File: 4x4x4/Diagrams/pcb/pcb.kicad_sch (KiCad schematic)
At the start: 78 parts, among them J1 Conn_01x04_Female, J10 Conn_01x04_Female, J11 Conn_01x04_Female, J12 Conn_01x04_Female, J13 Conn_01x04_Female, J14 Conn_01x04_Female, J2 Conn_01x06_Female, J3 Conn_01x04_Female, J4 Conn_01x04_Female, J5 Conn_01x04_Female, J6 Conn_01x04_Female, J7 Conn_01x04_Female, J8 Conn_01x04_Female, J9 Conn_01x04_Female, Q1 2N2219, Q2 2N2219, Q3 2N2219, Q4 2N2219, U1 74HC595, U2 74HC595, U3 74HC595, U4 74HC595, U5 74HC595, U6 74HC595, U7 74HC595

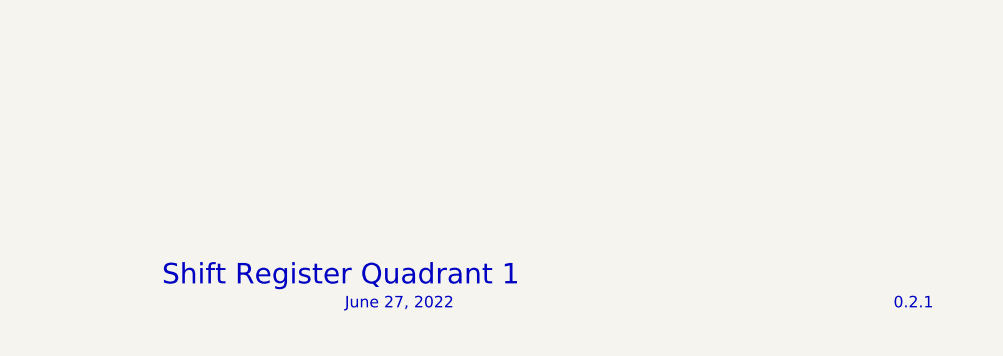
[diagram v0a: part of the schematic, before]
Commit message: revised quad 1 diagram
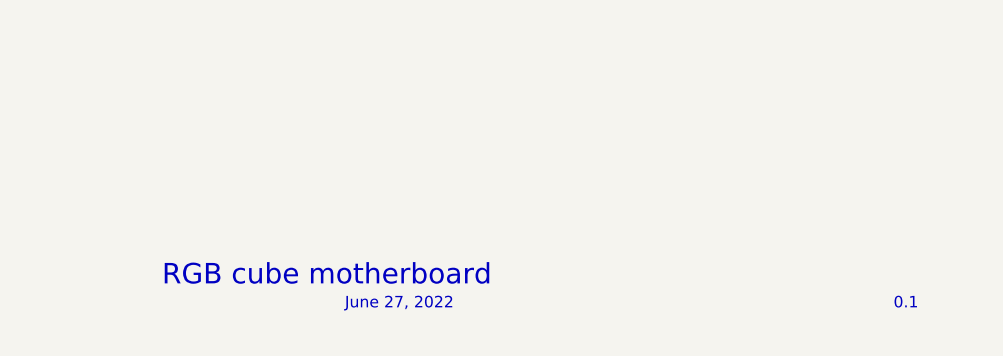
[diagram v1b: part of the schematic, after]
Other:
- note added: "0.1"
- note added: "RGB cube motherboard"
- note removed: "0.2.1"
- note removed: "Shift Register Quadrant 1"
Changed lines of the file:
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@@
     (stroke (width 0) (type default) (color 0 0 0 0))
   )
-  (text "Shift Register Quadrant 1 " (at 187.96 191.77 0)
+  (text "RGB cube motherboard" (at 187.96 191.77 0)
     (effects (font (size 2.27 2.27)) (justify left bottom))
   )
@@
     (effects (font (size 1.27 1.27)) (justify left bottom))
   )
-  (text "0.2.1" (at 269.24 194.31 0)
+  (text "0.1" (at 269.24 194.31 0)
     (effects (font (size 1.27 1.27)) (justify left bottom))
   )

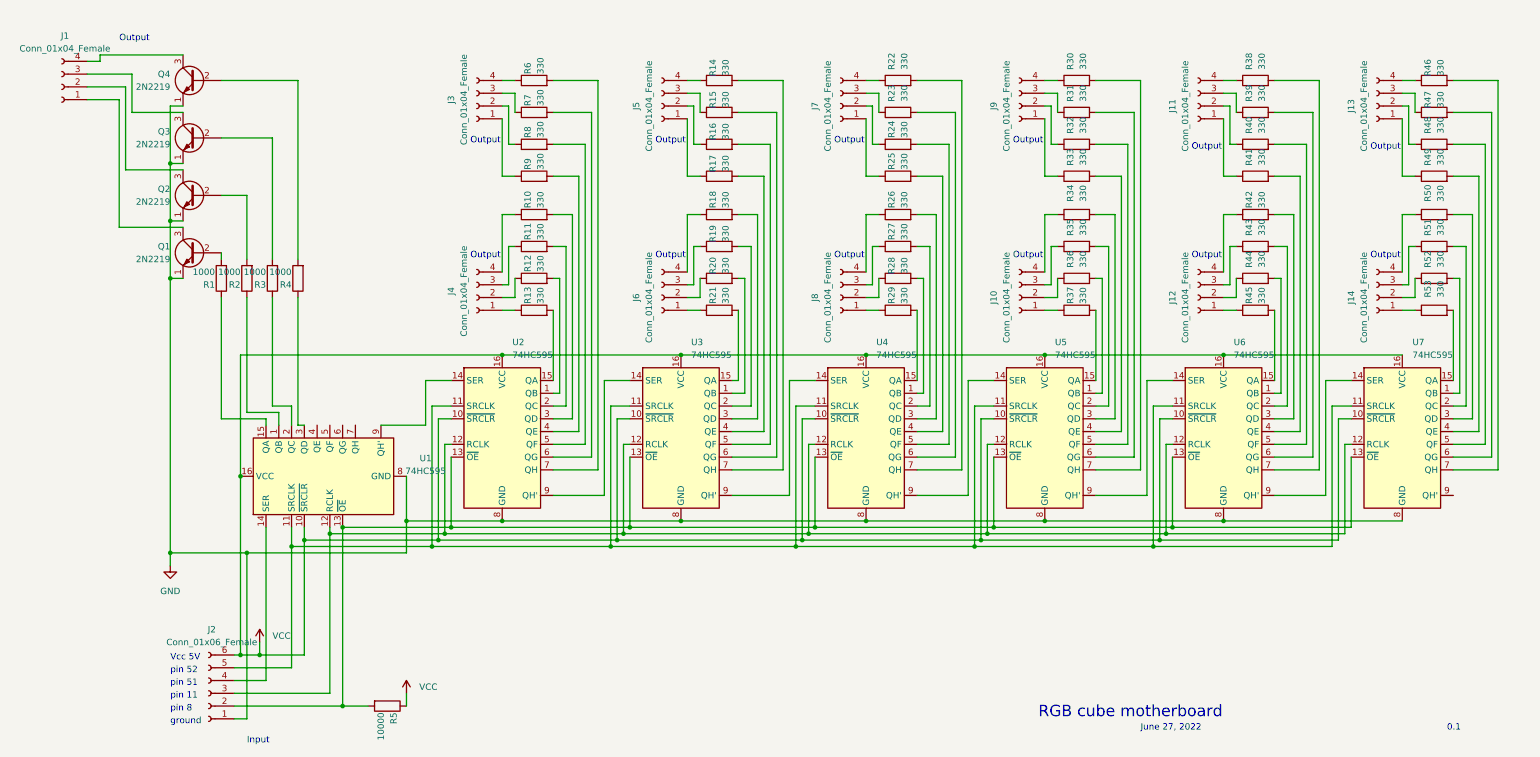
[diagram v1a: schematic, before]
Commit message: laying out 3d model of pcb
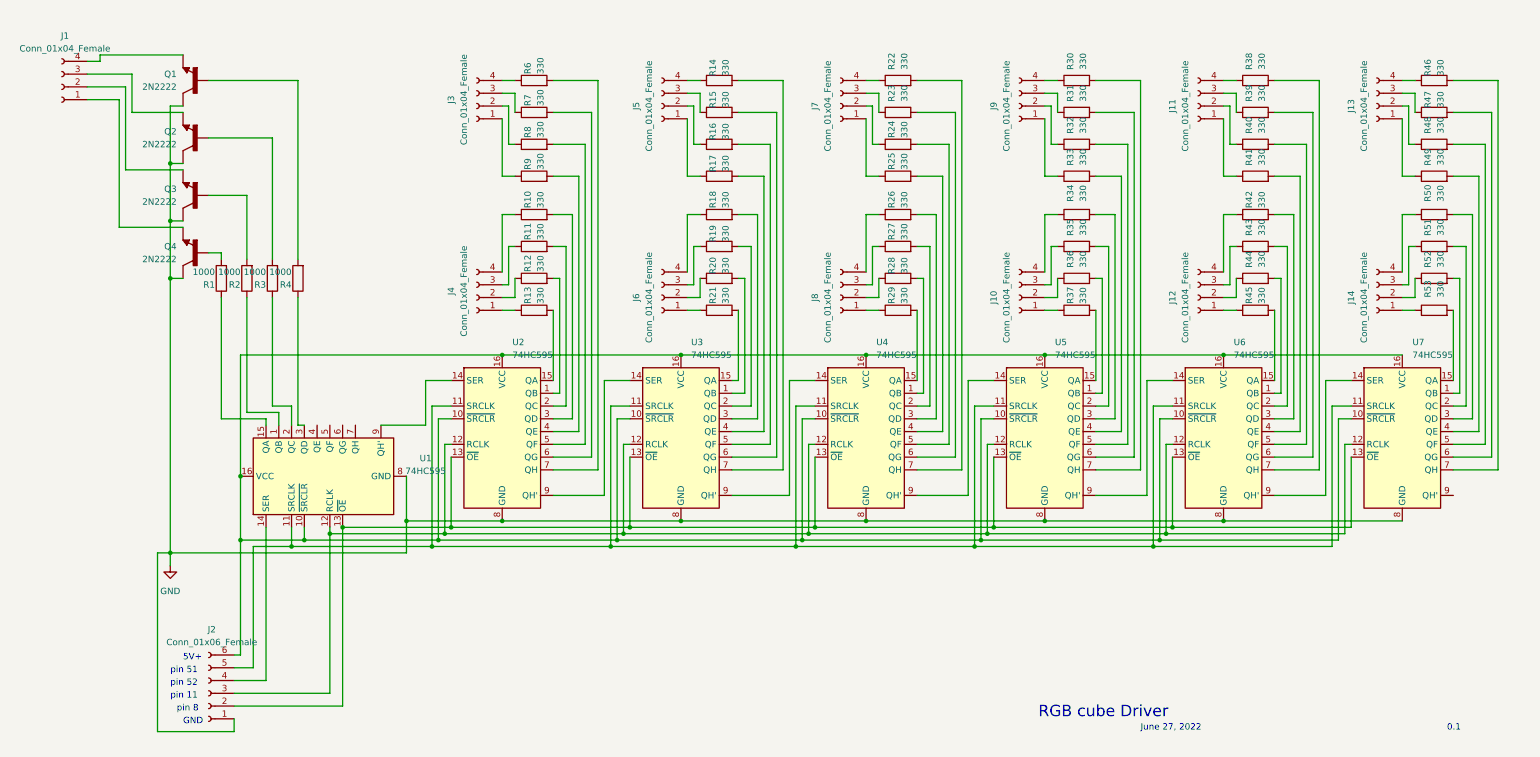
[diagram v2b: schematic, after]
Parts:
- removed Q1, Q2, Q3, Q4: 2N2219, Package_TO_SOT_THT:TO-39-3, symbol Transistor_BJT:2N2219
- removed R5: 10000, symbol Device:R
- added Q1, Q2, Q3, Q4: 2N2222, 2N2222:TO127P584H533-3, symbol 2N2222:2N2222
- J1, J10, J11, J12, J13, J14, J3, J4, J5, J6, J7, J8, J9: footprint (none) -> Connector_Molex:Molex_Micro-Fit_3.0_43650-0400_1x04_P3.00mm_Horizontal
- J2: footprint (none) -> Connector_Molex:Molex_Micro-Fit_3.0_43650-0600_1x06_P3.00mm_Horizontal
- R1, R10, R11, R12, R13, R14, R15, R16, R17, R18, R19, R2, R20, R21, R22, R23, R24, R25, R26, R27, R28, R29, R3, R30, R31, R32, R33, R34, R35, R36, R37, R38, R39, R4, R40, R41, R42, R43, R44, R45, R46, R47, R48, R49, R50, R51, R52, R53, R6, R7, R8, R9: footprint (none) -> Resistor_THT:R_Axial_DIN0204_L3.6mm_D1.6mm_P5.08mm_Horizontal
- U1, U2, U3, U4, U5, U6, U7: footprint (none) -> 74HC595:SO16
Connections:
- net GND: now also Q1.3, Q2.3, Q3.3, Q4.3
- net at J1.1 (Pin_1): now also Q4.1
- net at J1.2 (Pin_2): now also Q3.1
- net at J1.3 (Pin_3): now also Q2.1
- net at J1.4 (Pin_4): now also Q1.1
- net at R4.2: now also Q1.2
- net at R1.2: now also Q4.2
- net at R2.2: now also Q3.2
- net at R3.2: now also Q2.2
- net VCC: no longer names the net of J2.6 (Pin_6), U1.10 (~{SRCLR}), U1.16 (VCC), U2.10 (~{SRCLR}), U2.16 (VCC), U3.10 (~{SRCLR}), U3.16 (VCC), U4.10 (~{SRCLR}), U4.16 (VCC), U5.10 (~{SRCLR}), U5.16 (VCC), U6.10 (~{SRCLR}), U6.16 (VCC), U7.10 (~{SRCLR}), U7.16 (VCC)
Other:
- note added: "5V+"
- note added: "GND"
- note added: "RGB cube Driver"
- note removed: "Input"
- note removed: "Output"
- note removed: "RGB cube motherboard"
- note removed: "Vcc 5V"
- note removed: "ground"

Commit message: layout pcb complete
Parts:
- J1, J10, J11, J12, J13, J14, J3, J4, J5, J6, J7, J8, J9: footprint Connector_Molex:Molex_Micro-Fit_3.0_43650-0400_1x04_P3.00mm_Horizontal -> TerminalBlock_Phoenix:TerminalBlock_Phoenix_MKDS-1,5-4-5.08_1x04_P5.08mm_Horizontal
- J2: footprint Connector_Molex:Molex_Micro-Fit_3.0_43650-0600_1x06_P3.00mm_Horizontal -> TerminalBlock_Phoenix:TerminalBlock_Phoenix_PT-1,5-6-5.0-H_1x06_P5.00mm_Horizontal
- renumbered Q4 to Q1, Q3 to Q2, Q2 to Q3, Q1 to Q4

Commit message: review pcb
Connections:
- net at R4.1: now also U1.4 (QE); no longer U1.3 (QD)
- net at U1.12 (RCLK), U2.12 (RCLK), U3.12 (RCLK)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: now also J2.4 (Pin_4); no longer J2.3 (Pin_3)
- net at U1.13 (~{OE}), U2.13 (~{OE}), U3.13 (~{OE})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: now also J2.3 (Pin_3); no longer J2.2 (Pin_2)
- net at U1.1 (QB): now also R1.1; no longer R2.1
- net at U1.14 (SER): now also J2.2 (Pin_2); no longer J2.4 (Pin_4)
- net at U1.15 (QA): no longer R1.1
- net at U1.2 (QC): now also R2.1; no longer R3.1
- new net: R3.1, U1.3 (QD)

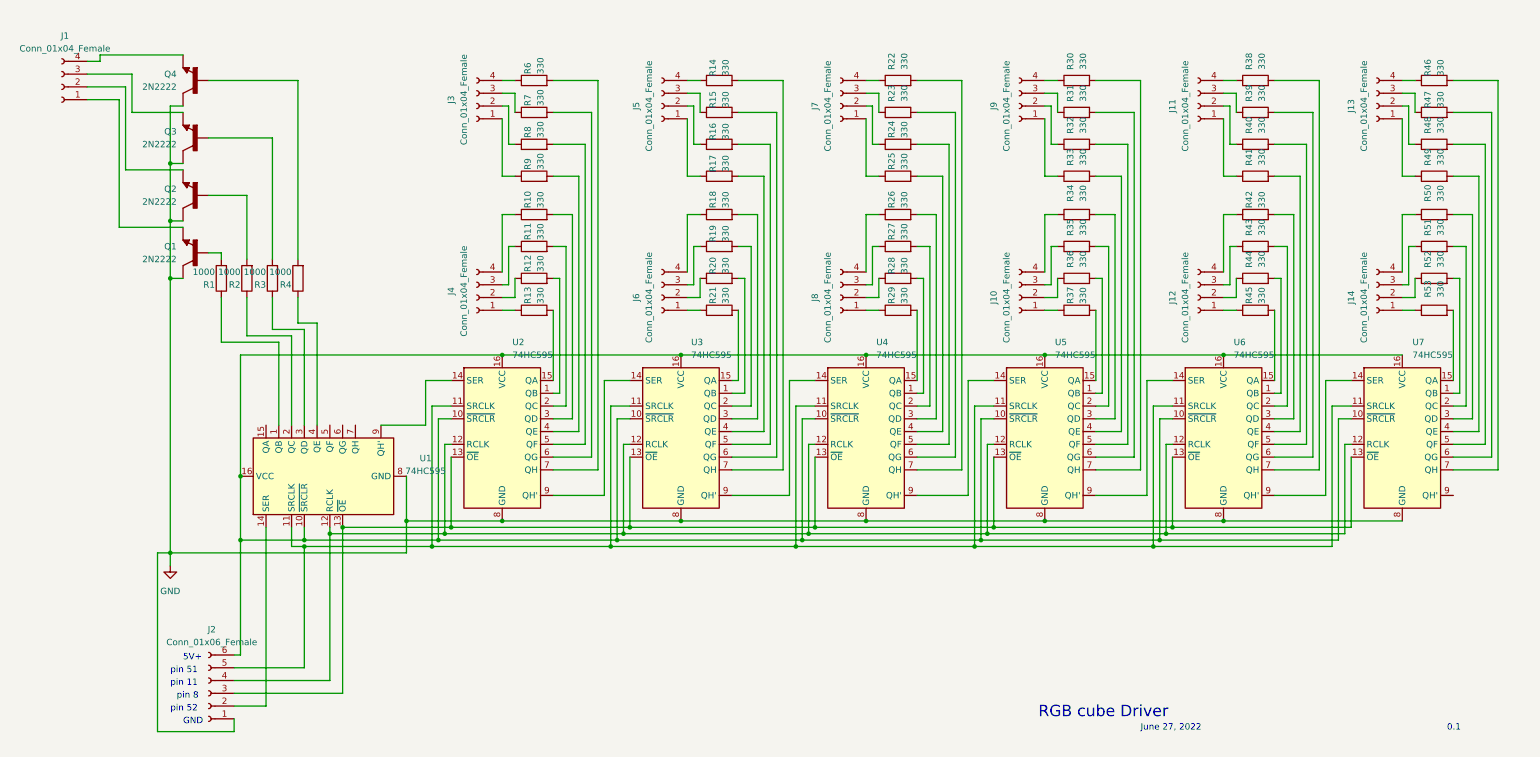
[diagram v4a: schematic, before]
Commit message: changed pcb symbols
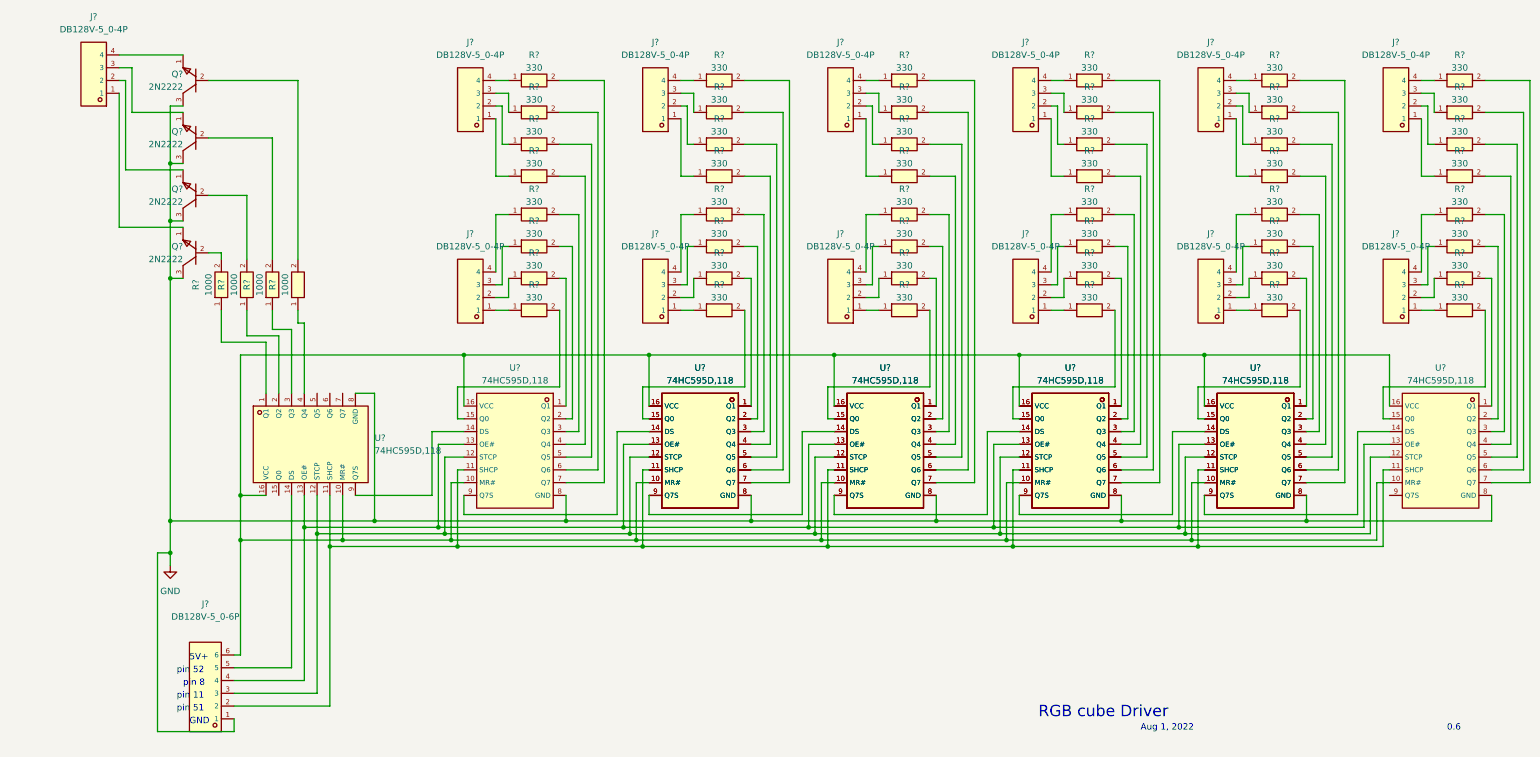
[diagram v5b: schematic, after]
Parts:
- removed J1, J10, J11, J12, J13, J14, J3, J4, J5, J6, J7, J8, J9: Conn_01x04_Female, TerminalBlock_Phoenix:TerminalBlock_Phoenix_MKDS-1,5-4-5.08_1x04_P5.08mm_Horizontal, symbol Connector:Conn_01x04_Female
- removed J2: Conn_01x06_Female, TerminalBlock_Phoenix:TerminalBlock_Phoenix_PT-1,5-6-5.0-H_1x06_P5.00mm_Horizontal, symbol Connector:Conn_01x06_Female
- removed Q1, Q2, Q3, Q4: 2N2222, 2N2222:TO127P584H533-3, symbol 2N2222:2N2222
- removed R1, R2, R3, R4: 1000, Resistor_THT:R_Axial_DIN0204_L3.6mm_D1.6mm_P5.08mm_Horizontal, symbol Device:R
- removed R10, R11, R12, R13, R14, R15, R16, R17, R18, R19, R20, R21, R22, R23, R24, R25, R26, R27, R28, R29, R30, R31, R32, R33, R34, R35, R36, R37, R38, R39, R40, R41, R42, R43, R44, R45, R46, R47, R48, R49, R50, R51, R52, R53, R6, R7, R8, R9: 330, Resistor_THT:R_Axial_DIN0204_L3.6mm_D1.6mm_P5.08mm_Horizontal, symbol Device:R
- removed U1, U2, U3, U4, U5, U6, U7: 74HC595, 74HC595:SO16, symbol 74xx:74HC595
- added J? (x13): DB128V-5_0-4P, footprint:CONN-TH_DB128V-5.0-4P, symbol DB128V-5.0-4P-GN-S:DB128V-5_0-4P
- added J?: DB128V-5_0-6P, footprint:CONN-TH_6P-P5.00_DB128V, symbol DB128V-5.0-6P-GN-S:DB128V-5_0-6P
- added Q? (x4): 2N2222, footprint:TO-92-3_L4.9-W3.7-P1.27-L, symbol 2N2222A:2N2222
- added R? (x48): 330, footprint:RES-TH_BD2.4-L6.3-P10.30-D0.6, symbol 330R:RD_1_2WS_330R_J_T_B_A1
- added R? (x4): 1000, footprint:RES-TH_BD2.4-L6.3-P10.30-D0.6, symbol 1kR:RD_1_2WS_1K_J_T_B_A1
- added U? (x11): 74HC595D,118, footprint:SOIC-16_L9.9-W3.9-P1.27-LS6.0-BL, symbol 74HC595D,118:74HC595D,118
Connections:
- net GND: now also J?.1, Q?.3 (C), Q?.3 (C), Q?.3 (C), Q?.3 (C), U?.8 (GND), U?.8 (GND), U?.8 (GND), U?.8 (GND), U?.8 (GND), U?.8 (GND), U?.8 (GND), U?.8 (GND), U?.8 (GND), U?.8 (GND), U?.8 (GND)
- new net: J?.1, R?.1 (x12)
- new net: J?.2, R?.1 (x12)
- new net: J?.3, R?.1 (x12)
- new net: J?.4, R?.1 (x12)
- new net: R?.2, U?.5 (Q5), U?.5 (Q5) (x4)
- new net: R?.2, U?.1 (Q1), U?.1 (Q1) (x4)
- new net: R?.2, U?.2 (Q2) (x2)
- new net: R?.2, U?.1 (Q1) (x2)
- new net: R?.2, U?.7 (Q7), U?.7 (Q7) (x4)
- new net: J?.6, U?.10 (MR#), U?.10 (MR#), U?.10 (MR#), U?.10 (MR#), U?.10 (MR#), U?.10 (MR#), U?.10 (MR#), U?.10 (MR#), U?.10 (MR#), U?.10 (MR#), U?.10 (MR#), U?.16 (VCC), U?.16 (VCC), U?.16 (VCC), U?.16 (VCC), U?.16 (VCC), U?.16 (VCC), U?.16 (VCC), U?.16 (VCC), U?.16 (VCC), U?.16 (VCC), U?.16 (VCC)
- new net: J?.2, U?.11 (SHCP), U?.11 (SHCP), U?.11 (SHCP), U?.11 (SHCP), U?.11 (SHCP), U?.11 (SHCP), U?.11 (SHCP), U?.11 (SHCP), U?.11 (SHCP), U?.11 (SHCP), U?.11 (SHCP)
- new net: J?.3, U?.12 (STCP), U?.12 (STCP), U?.12 (STCP), U?.12 (STCP), U?.12 (STCP), U?.12 (STCP), U?.12 (STCP), U?.12 (STCP), U?.12 (STCP), U?.12 (STCP), U?.12 (STCP)
- new net: J?.4, U?.13 (OE#), U?.13 (OE#), U?.13 (OE#), U?.13 (OE#), U?.13 (OE#), U?.13 (OE#), U?.13 (OE#), U?.13 (OE#), U?.13 (OE#), U?.13 (OE#), U?.13 (OE#)
- new net: U?.14 (DS), U?.14 (DS), U?.9 (Q7S), U?.9 (Q7S) (x3)
- new net: R?.2, U?.15 (Q0), U?.15 (Q0) (x4)
- new net: R?.2, U?.2 (Q2), U?.2 (Q2) (x4)
- new net: R?.2, U?.3 (Q3), U?.3 (Q3) (x4)
- new net: R?.2, U?.4 (Q4), U?.4 (Q4) (x4)
- new net: R?.2, U?.6 (Q6), U?.6 (Q6) (x4)
- new net: U?.14 (DS), U?.9 (Q7S), U?.9 (Q7S)
- new net: R?.2, U?.7 (Q7) (x2)
- new net: J?.5, U?.14 (DS)
- new net: U?.14 (DS), U?.14 (DS), U?.9 (Q7S)
- new net: R?.2, U?.6 (Q6) (x2)
- new net: R?.2, U?.3 (Q3) (x2)
- new net: R?.2, U?.5 (Q5) (x2)
- new net: R?.1, U?.1 (Q1)
- new net: R?.1, U?.2 (Q2)
- new net: R?.1, U?.3 (Q3)
- new net: R?.1, U?.4 (Q4)
- new net: U?.14 (DS), U?.9 (Q7S)
- new net: R?.2, U?.4 (Q4) (x2)
- new net: R?.2, U?.15 (Q0) (x2)
- new net: Q?.2 (B), R?.2 (x4)
- new net: J?.1, Q?.1 (E)
- new net: J?.3, Q?.1 (E)
- new net: J?.2, Q?.1 (E)
- new net: J?.4, Q?.1 (E)
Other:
- note added: "0.6"
- note added: "Aug 1, 2022"
- note removed: "0.1"
- note removed: "June 27, 2022"
